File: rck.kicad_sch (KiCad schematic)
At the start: 40 parts, among them J01 Conn_02x22_Row_Letter_Last, J02 Conn_02x22_Row_Letter_Last, J03 Conn_02x22_Row_Letter_Last, J04 Conn_02x22_Row_Letter_Last

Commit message: V1.0Rack
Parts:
- added J5: Conn_01x02_Pin, Connector_PinHeader_2.54mm:PinHeader_1x02_P2.54mm_Vertical, symbol Connector:Conn_01x02_Pin
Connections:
- net VCC: now also J5.1 (Pin_1)
- net GND: now reaches J01.22a (Pin_22a)
- net GND: now also J5.2 (Pin_2)
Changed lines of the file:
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@@
+      )
+    )
+    (symbol "power:GND" (power) (pin_names (offset 0)) (in_bom yes) (on_board yes)
+      (property "Reference" "#PWR" (at 0 -6.35 0)
+        (effects (font (size 1.27 1.27)) hide)
+      )
+      (property "Value" "GND" (at 0 -3.81 0)
+        (effects (font (size 1.27 1.27)))
+      )
+      (property "Footprint" "" (at 0 0 0)
+        (effects (font (size 1.27 1.27)) hide)
+      )
+      (property "Datasheet" "" (at 0 0 0)
+        (effects (font (size 1.27 1.27)) hide)
+      )
+      (property "ki_keywords" "global power" (at 0 0 0)
+        (effects (font (size 1.27 1.27)) hide)
+      )
+      (property "ki_description" "Power symbol creates a global label with name \"GND\" , ground" (at 0 0 0)
+        (effects (font (size 1.27 1.27)) hide)
+      )
+      (symbol "GND_0_1"
+        (polyline
+          (pts
+            (xy 0 0)
+            (xy 0 -1.27)
+            (xy 1.27 -1.27)
+            (xy 0 -2.54)
+            (xy -1.27 -1.27)
+            (xy 0 -1.27)
+          )
+          (stroke (width 0) (type default))
+          (fill (type none))
+        )
+      )
+      (symbol "GND_1_1"
+        (pin power_in line (at 0 0 270) (length 0) hide
+          (name "GND" (effects (font (size 1.27 1.27))))
+          (number "1" (effects (font (size 1.27 1.27))))
+        )
       )
     )
@@
     (stroke (width 0) (type default))
   )
+  (wire (pts (xy 41.91 153.67) (xy 46.99 153.67))
+    (stroke (width 0) (type default))
+  )
   (wire (pts (xy 91.44 66.04) (xy 80.01 66.04))
     (stroke (width 0) (type default))
@@
     (stroke (width 0) (type default))
   )
+  (wire (pts (xy 165.1 55.88) (xy 165.1 57.15))
+    (stroke (width 0) (type default))
+  )
   (wire (pts (xy 175.26 81.28) (xy 186.69 81.28))
     (stroke (width 0) (type default))
@@
     (stroke (width 0) (type default))
   )
+  (wire (pts (xy 156.21 55.88) (xy 165.1 55.88))
+    (stroke (width 0) (type default))
+  )
   (wire (pts (xy 194.31 102.87) (xy 194.31 91.44))
     (stroke (width 0) (type default))
@@
     (stroke (width 0) (type default))
   )
+  (wire (pts (xy 46.99 149.86) (xy 46.99 153.67))
+    (stroke (width 0) (type default))
+  )
   (wire (pts (xy 118.11 119.38) (xy 121.92 119.38))
     (stroke (width 0) (type default))
@@
     (stroke (width 0) (type default))
   )
+  (wire (pts (xy 41.91 156.21) (xy 46.99 156.21))
+    (stroke (width 0) (type default))
+  )
   (wire (pts (xy 220.98 102.87) (xy 226.06 102.87))
     (stroke (width 0) (type default))
@@
   )
   (wire (pts (xy 213.36 133.35) (xy 186.69 133.35))
+    (stroke (width 0) (type default))
+  )
+  (wire (pts (xy 46.99 156.21) (xy 46.99 158.75))
     (stroke (width 0) (type default))
   )
@@
     )
   )
+  (symbol (lib_id "power:GND") (at 165.1 57.15 0) (unit 1)
+    (in_bom yes) (on_board yes) (dnp no) (fields_autoplaced)
+    (property "Reference" "#PWR08" (at 165.1 63.5 0)
+      (effects (font (size 1.27 1.27)) hide)
+    )
+    (property "Value" "GND" (at 165.1 62.23 0)
+      (effects (font (size 1.27 1.27)))
+    )
+    (property "Footprint" "" (at 165.1 57.15 0)
+      (effects (font (size 1.27 1.27)) hide)
+    )
+    (property "Datasheet" "" (at 165.1 57.15 0)
+      (effects (font (size 1.27 1.27)) hide)
+    )
+    (pin "1")
+    (instances
+      (project "rck"
+        (path "/02cabdf2-0231-47a4-9c5b-3124e84f3136"
+          (reference "#PWR08") (unit 1)
+        )
+      )
+    )
+  )
   (symbol (lib_id "Device:LED") (at 217.17 52.07 0) (unit 1)
     (in_bom yes) (on_board yes) (dnp no)
@@
     )
   )
+  (symbol (lib_id "power:GND") (at 46.99 158.75 0) (unit 1)
+    (in_bom yes) (on_board yes) (dnp no) (fields_autoplaced)
+    (property "Reference" "#PWR07" (at 46.99 165.1 0)
+      (effects (font (size 1.27 1.27)) hide)
+    )
+    (property "Value" "GND" (at 46.99 163.83 0)
+      (effects (font (size 1.27 1.27)))
+    )
+    (property "Footprint" "" (at 46.99 158.75 0)
+      (effects (font (size 1.27 1.27)) hide)
+    )
+    (property "Datasheet" "" (at 46.99 158.75 0)
+      (effects (font (size 1.27 1.27)) hide)
+    )
+    (pin "1")
+    (instances
+      (project "rck"
+        (path "/02cabdf2-0231-47a4-9c5b-3124e84f3136"
+          (reference "#PWR07") (unit 1)
+        )
+      )
+    )
+  )
   (symbol (lib_id "Device:R") (at 229.87 77.47 90) (unit 1)
     (in_bom yes) (on_board yes) (dnp no)
@@
     )
   )
+  (symbol (lib_id "Connector:Conn_01x02_Pin") (at 36.83 153.67 0) (unit 1)
+    (in_bom yes) (on_board yes) (dnp no) (fields_autoplaced)
+    (property "Reference" "J5" (at 37.465 148.59 0)
+      (effects (font (size 1.27 1.27)))
+    )
+    (property "Value" "Conn_01x02_Pin" (at 37.465 151.13 0)
+      (effects (font (size 1.27 1.27)))
+    )
+    (property "Footprint" "Connector_PinHeader_2.54mm:PinHeader_1x02_P2.54mm_Vertical" (at 36.83 153.67 0)
+      (effects (font (size 1.27 1.27)) hide)
+    )
+    (property "Datasheet" "~" (at 36.83 153.67 0)
+      (effects (font (size 1.27 1.27)) hide)
+    )
+    (pin "1")
+    (pin "2")
+    (instances
+      (project "rck"
+        (path "/02cabdf2-0231-47a4-9c5b-3124e84f3136"
+          (reference "J5") (unit 1)
+        )
+      )
+    )
+  )
   (symbol (lib_id "Device:R") (at 229.87 92.71 90) (unit 1)
     (in_bom yes) (on_board yes) (dnp no)
@@
         )
       )
+    )
+  )
+  (symbol (lib_id "power:VCC") (at 46.99 149.86 0) (unit 1)
+    (in_bom yes) (on_board yes) (dnp no) (fields_autoplaced)
+    (property "Reference" "#PWR06" (at 46.99 153.67 0)
+      (effects (font (size 1.27 1.27)) hide)
+    )
+    (property "Value" "VCC" (at 46.99 144.78 0)
+      (effects (font (size 1.27 1.27)))
+    )
+    (property "Footprint" "" (at 46.99 149.86 0)
+      (effects (font (size 1.27 1.27)) hide)
+    )
+    (property "Datasheet" "" (at 46.99 149.86 0)
+      (effects (font (size 1.27 1.27)) hide)
+    )
+    (pin "1")
+    (instances
+      (project "rck"
+        (path "/02cabdf2-0231-47a4-9c5b-3124e84f3136"
+          (reference "#PWR06") (unit 1)
+        )
+      )

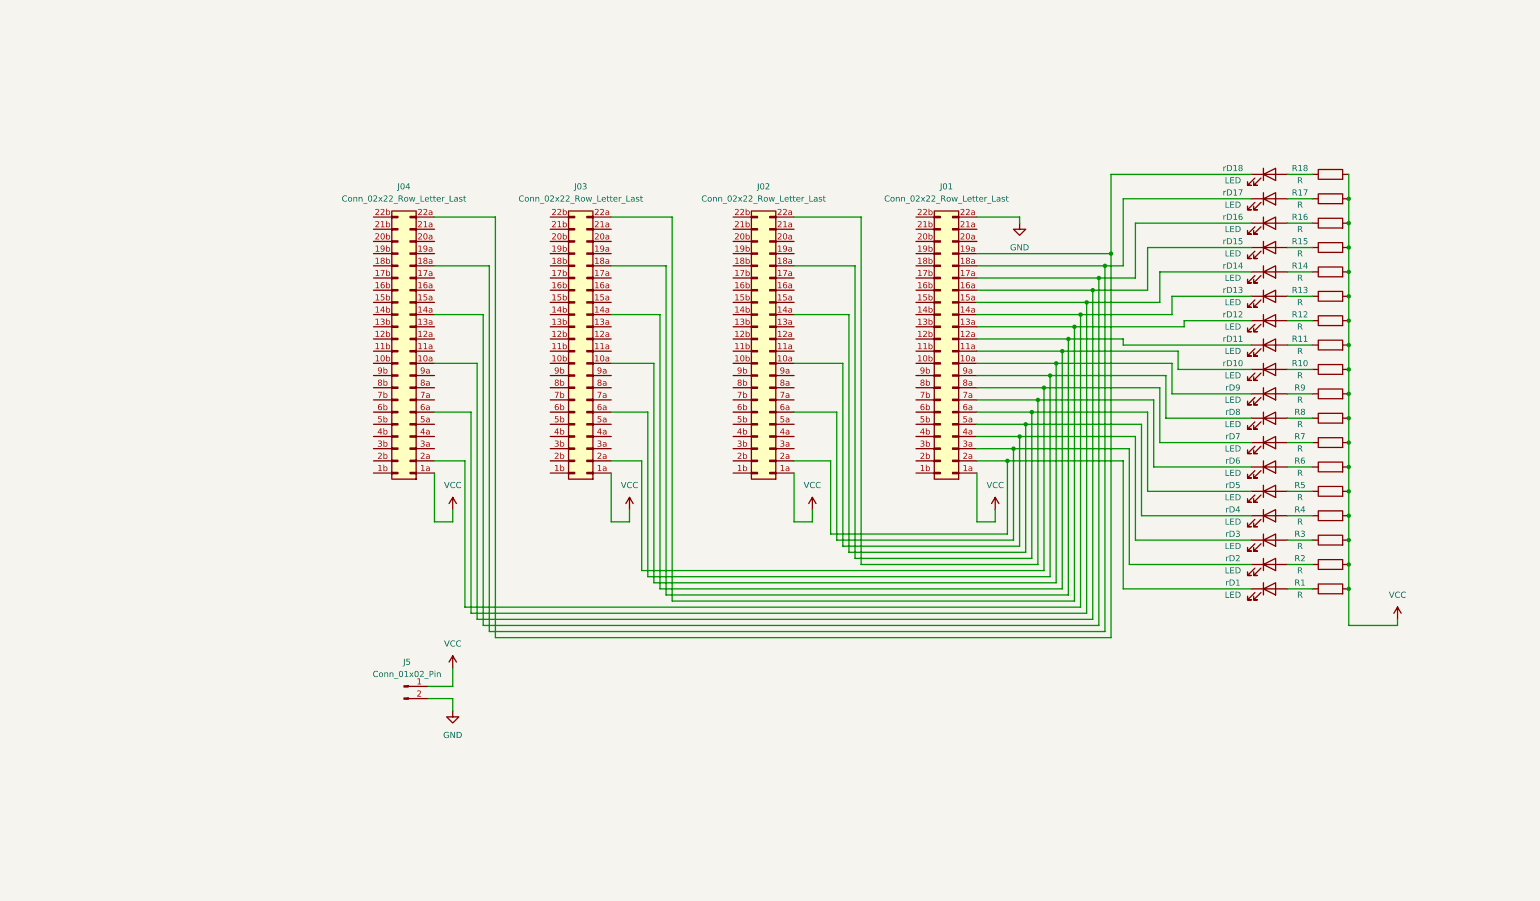
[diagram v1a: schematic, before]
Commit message: v2Reg12v
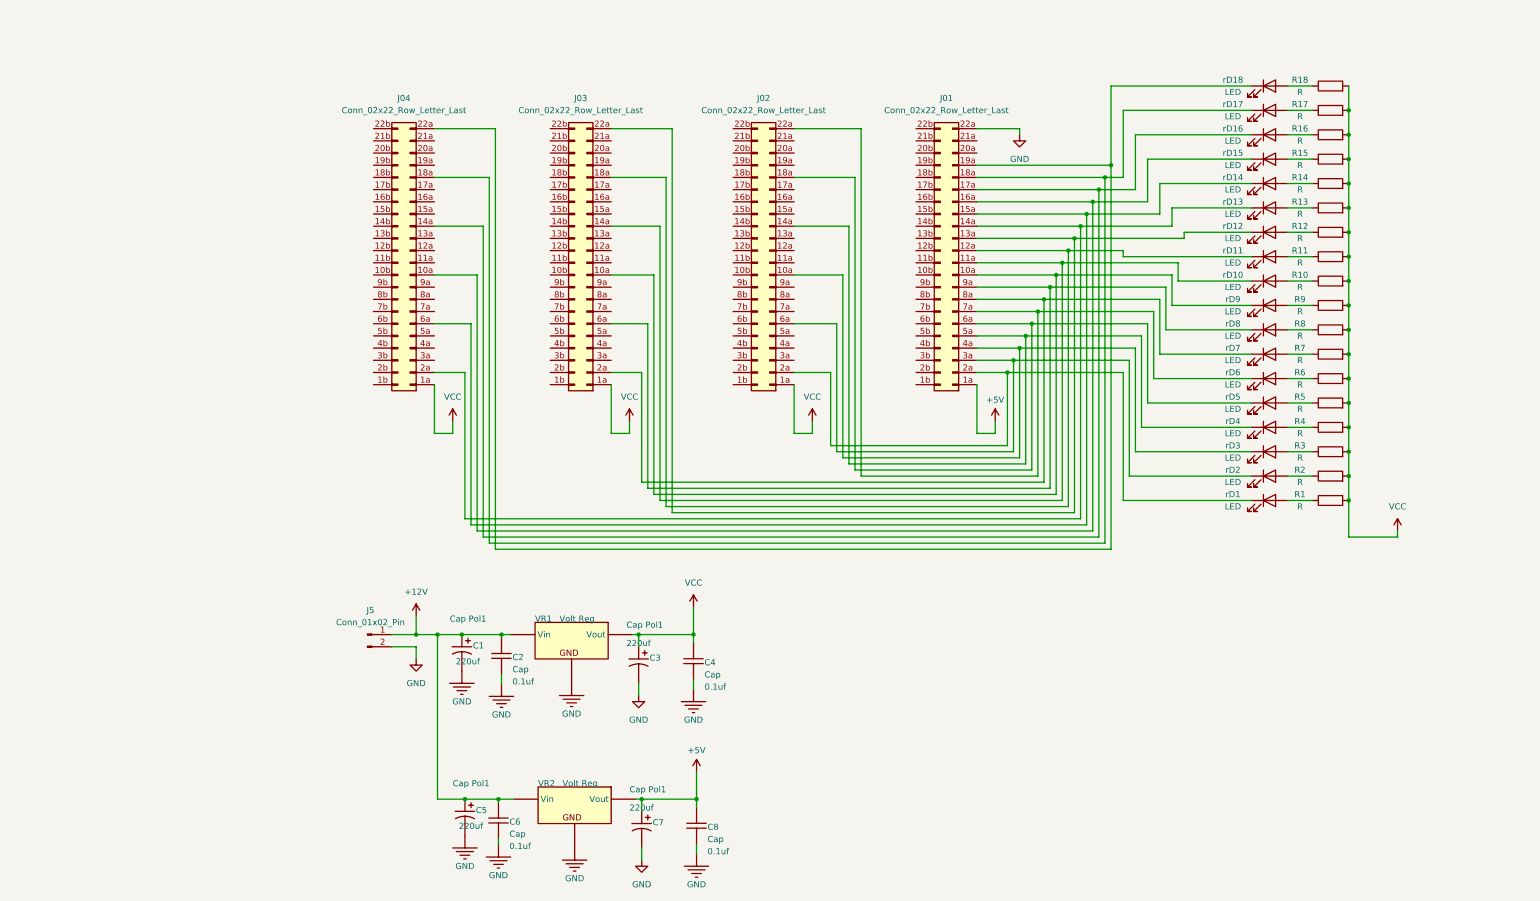
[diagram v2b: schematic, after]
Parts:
- added C1, C3, C5, C7: Cap Pol1, Capacitor_SMD:CP_Elec_5x5.9, symbol controlSemaforico-altium-import:root_3_Cap Pol1
- added C2, C4, C6, C8: Cap, Capacitor_SMD:C_1210_3225Metric, symbol controlSemaforico-altium-import:root_1_Cap
- added VR1, VR2: Volt Reg, Package_TO_SOT_SMD:TO-252-3_TabPin2, symbol controlSemaforico-altium-import:root_0_Volt Reg
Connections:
- net GND: now also C1.2, C2.1, C3.2, C4.1, C5.2, C6.1, C7.2, C8.1, VR1.2 (GND), VR2.2 (GND)
- net VCC: now also C3.1, C4.2, VR1.3 (Vout); no longer J01.1a (Pin_1a), J5.1 (Pin_1)
- new net +12V: C1.1, C2.2, C5.1, C6.2, J5.1 (Pin_1), VR1.1 (Vin), VR2.1 (Vin)
- new net +5V: C7.1, C8.2, J01.1a (Pin_1a), VR2.3 (Vout)
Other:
- moved on the sheet: J01, J02, J03, J04, J5, R1, R10, R11, R12, R13, R14, R15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

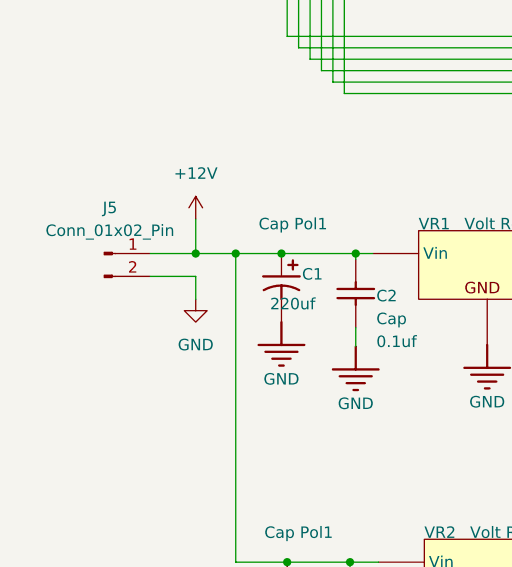
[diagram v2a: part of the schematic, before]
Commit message: v2Reg12vMolex
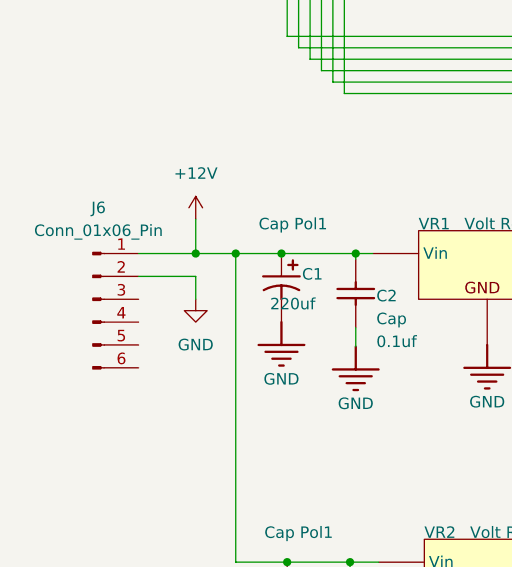
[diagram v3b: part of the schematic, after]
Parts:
- removed J5: Conn_01x02_Pin, Connector_PinHeader_2.54mm:PinHeader_1x02_P2.54mm_Vertical, symbol Connector:Conn_01x02_Pin
- added J6: Conn_01x06_Pin, Connector_PinSocket_2.54mm:PinSocket_1x06_P2.54mm_Vertical, symbol Connector:Conn_01x06_Pin
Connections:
- net +12V: now also J6.1 (Pin_1)
- net GND: now also J6.2 (Pin_2)
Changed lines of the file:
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@@
   (junction (at 173.99 65.405) (diameter 0) (color 0 0 0 0)
   )
+  (junction (at 39.37 142.875) (diameter 0) (color 0 0 0 0)
+  )
   (junction (at 175.26 62.865) (diameter 0) (color 0 0 0 0)
   )
@@
   (junction (at 85.725 142.875) (diameter 0) (color 0 0 0 0)
   )
-  (junction (at 39.37 142.875) (diameter 0) (color 0 0 0 0)
-  )
   (junction (at 181.61 50.165) (diameter 0) (color 0 0 0 0)
   )
@@
   )
   (wire (pts (xy 88.9 113.665) (xy 88.9 67.945))
-    (stroke (width 0) (type default))
-  )
-  (wire (pts (xy 34.29 142.875) (xy 39.37 142.875))
     (stroke (width 0) (type default))
   )
@@
     (stroke (width 0) (type default))
   )
-  (wire (pts (xy 34.29 145.415) (xy 39.37 145.415))
-    (stroke (width 0) (type default))
-  )
   (wire (pts (xy 220.98 84.455) (xy 226.06 84.455))
     (stroke (width 0) (type default))
@@
     (stroke (width 0) (type default))
   )
+  (wire (pts (xy 33.02 142.875) (xy 39.37 142.875))
+    (stroke (width 0.254) (type default))
+  )
   (wire (pts (xy 220.98 59.055) (xy 226.06 59.055))
     (stroke (width 0) (type default))
@@
     (stroke (width 0) (type default))
   )
+  (wire (pts (xy 33.02 145.415) (xy 39.37 145.415))
+    (stroke (width 0) (type default))
+  )
   (wire (pts (xy 92.71 117.475) (xy 92.71 37.465))
     (stroke (width 0) (type default))
@@
         (path "/02cabdf2-0231-47a4-9c5b-3124e84f3136"
           (reference "rD11") (unit 1)
+        )
+      )
+    )
+  )
+  (symbol (lib_id "Connector:Conn_01x06_Pin") (at 27.94 147.955 0) (unit 1)
+    (in_bom yes) (on_board yes) (dnp no) (fields_autoplaced)
+    (property "Reference" "J6" (at 28.575 137.795 0)
+      (effects (font (size 1.27 1.27)))
+    )
+    (property "Value" "Conn_01x06_Pin" (at 28.575 140.335 0)
+      (effects (font (size 1.27 1.27)))
+    )
+    (property "Footprint" "Connector_PinSocket_2.54mm:PinSocket_1x06_P2.54mm_Vertical" (at 27.94 147.955 0)
+      (effects (font (size 1.27 1.27)) hide)
+    )
+    (property "Datasheet" "~" (at 27.94 147.955 0)
+      (effects (font (size 1.27 1.27)) hide)
+    )
+    (pin "1")
+    (pin "6")
+    (pin "3")
+    (pin "4")
+    (pin "5")
+    (pin "2")
+    (instances
+      (project "rck"
+        (path "/02cabdf2-0231-47a4-9c5b-3124e84f3136"
+          (reference "J6") (unit 1)
         )
       )
@@
         )
       )
-    )
-  )
-  (symbol (lib_id "Connector:Conn_01x02_Pin") (at 29.21 142.875 0) (unit 1)
-    (in_bom yes) (on_board yes) (dnp no) (fields_autoplaced)
-    (property "Reference" "J5" (at 29.845 137.795 0)
-      (effects (font (size 1.27 1.27)))
-    )
-    (property "Value" "Conn_01x02_Pin" (at 29.845 140.335 0)
-      (effects (font (size 1.27 1.27)))
-    )
-    (property "Footprint" "Connector_PinHeader_2.54mm:PinHeader_1x02_P2.54mm_Vertical" (at 29.21 142.875 0)
-      (effects (font (size 1.27 1.27)) hide)
-    )
-    (property "Datasheet" "~" (at 29.21 142.875 0)
-      (effects (font (size 1.27 1.27)) hide)
-    )
-    (pin "1")
-    (pin "2")
-    (instances
-      (project "rck"
-        (path "/02cabdf2-0231-47a4-9c5b-3124e84f3136"
-          (reference "J5") (unit 1)
-        )
-      )

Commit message: corrección5V
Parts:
- VR2: footprint Package_TO_SOT_SMD:TO-252-3_TabPin2 -> Package_TO_SOT_SMD:TO-263-2

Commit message: cambio de 7805
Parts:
- VR2: footprint Package_TO_SOT_SMD:TO-263-2 -> Package_TO_SOT_THT:TO-220-3_Vertical
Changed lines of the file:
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@@
 			)
 		)
-		(property "Footprint" "Package_TO_SOT_SMD:TO-263-2"
+		(property "Footprint" "Package_TO_SOT_THT:TO-220-3_Vertical"
 			(at 72.39 167.005 0)
 			(effects

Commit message: 10F Connected
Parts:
- added J5, J6: Conn_02x22_Row_Letter_Last, Library:Edac_22x2_3.96, symbol Connector_Generic:Conn_02x22_Row_Letter_Last
- J1: renamed from J01; footprint EdgeConectors:Edac_22x2_3.96 -> Library:Edac_22x2_3.96
- J2: renamed from J02; footprint EdgeConectors:Edac_22x2_3.96 -> Library:Edac_22x2_3.96
- J3: renamed from J03; footprint EdgeConectors:Edac_22x2_3.96 -> Library:Edac_22x2_3.96
- J4: renamed from J04; footprint EdgeConectors:Edac_22x2_3.96 -> Library:Edac_22x2_3.96
- renumbered J6 to J7
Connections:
- net VCC: now also J5.1a (Pin_1a), J6.1a (Pin_1a)
- net A6-04: now reaches J1.10b (Pin_10b)
- net A6-04: now also J6.14a (Pin_14a)
- net A6-05: now reaches J1.11b (Pin_11b)
- net A6-05: now also J6.18a (Pin_18a)
- net A6-06: now reaches J1.12b (Pin_12b)
- net A6-06: now also J6.22a (Pin_22a)
- net A5-01: now reaches J1.1b (Pin_1b)
- net A5-01: now also J5.2a (Pin_2a)
- net A5-02: now reaches J1.2b (Pin_2b)
- net A5-02: now also J5.6a (Pin_6a)
- net A5-03: now reaches J1.3b (Pin_3b)
- net A5-03: now also J5.10a (Pin_10a)
- net A5-04: now reaches J1.4b (Pin_4b)
- net A5-04: now also J5.14a (Pin_14a)
- net A5-05: now reaches J1.5b (Pin_5b)
- net A5-05: now also J5.18a (Pin_18a)
- net A5-06: now reaches J1.6b (Pin_6b)
- net A5-06: now also J5.22a (Pin_22a)
- net A6-01: now reaches J1.7b (Pin_7b)
- net A6-01: now also J6.2a (Pin_2a)
- net A6-02: now reaches J1.8b (Pin_8b)
- net A6-02: now also J6.6a (Pin_6a)
- net A6-03: now reaches J1.9b (Pin_9b)
- net A6-03: now also J6.10a (Pin_10a)
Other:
- moved on the sheet: J1, J2, J3, J4
